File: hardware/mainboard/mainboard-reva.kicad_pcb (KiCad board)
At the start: 4 copper layers, 88 x 48 mm, 77 parts, among them J1 USB-C, J2 BATTERY, J3 SM05B-GHS-TB / ENCODER, J4 SM03B-GHS-TB / SNOOZE, J5 Molex 54550-2472 / GDEY037T03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, J6 Molex 54550-0672 / FL21 front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, J7 SPEAKER, J8 SM02B-GHS-TB / WAKE_LED, Q2 AO3400A / WAKE, U1 ESP32-S3-WROOM-1-N8, U2 BQ24074RGTR, U3 TPS62840DLCR, U4 RV-3028-C7, U5 VEML7700, U6 MAX98357AETE+T, U7 USBLC6-2SC6

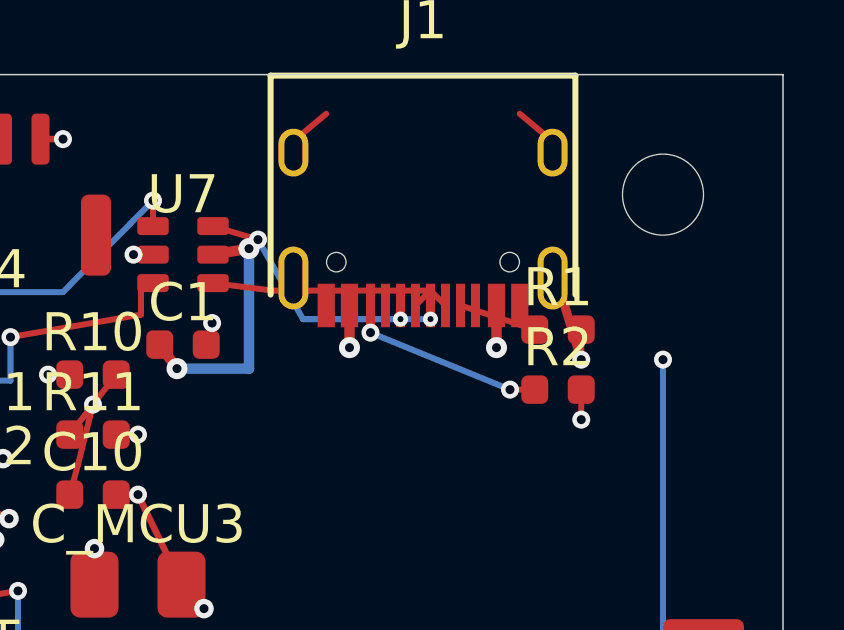
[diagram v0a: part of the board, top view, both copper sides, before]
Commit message: fix(mainboard): clean USB-C breakout lanes and CC placement
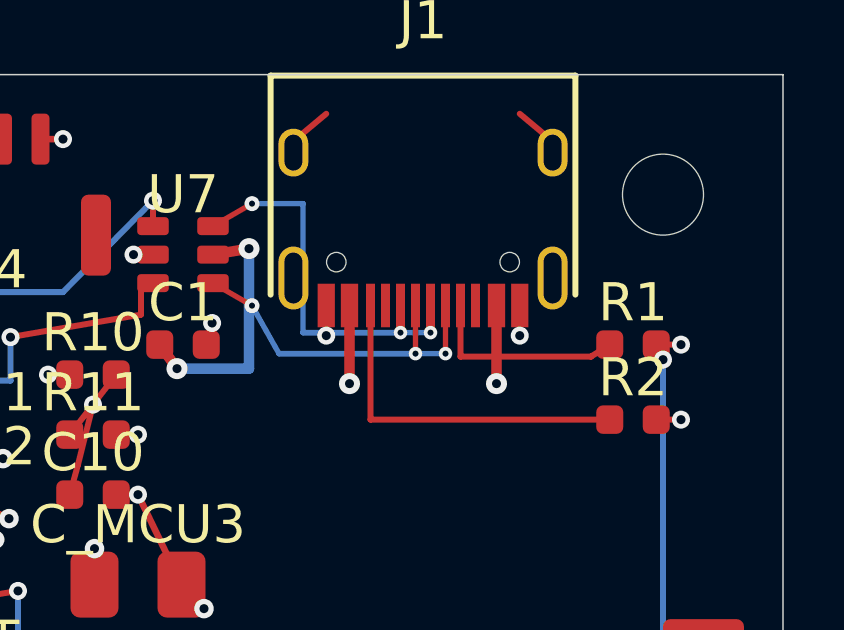
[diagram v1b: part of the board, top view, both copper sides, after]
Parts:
- moved R2 2.69 mm to (83.0, 11.5)
- moved R1 2.55 mm to (83.0, 9.00)
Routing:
- net USB_D-_CONN: track 8.67 -> 16.6 mm, vias 0 -> 3
- net USB_CC2: track 6.75 -> 11.8 mm, vias 2 -> 0
- net USB_CC1: track 2.60 -> 6.80 mm
- net USB_D+_CONN: track 13.0 -> 16.8 mm
- net VBUS_USB: track 90.6 -> 94.0 mm
- net GND: track 105.7 -> 104.1 mm, vias 52 -> 54
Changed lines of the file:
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@@
     (pad "6" smd roundrect (at 1 -0.95) (size 1.05 0.6) (layers "F.Cu" "F.Paste" "F.Mask") (roundrect_rratio 0.2) (net 59 "USB_D+_CONN"))
   )
-  (footprint "Resistor_SMD:R_0603_1608Metric" (layer "F.Cu") (at 80.5 8.5)
+  (footprint "Resistor_SMD:R_0603_1608Metric" (layer "F.Cu") (at 83.0 9.0)
     (property "Reference" "R1" (at 0 -1.4) (layer "F.SilkS"))
     (property "Value" "5.1k CC1" (at 0 1.4) (layer "F.Fab") hide)
@@
     (pad "2" smd roundrect (at 0.775 0) (size 0.9 0.95) (layers "F.Cu" "F.Paste" "F.Mask") (roundrect_rratio 0.25) (net 1 "GND"))
   )
-  (footprint "Resistor_SMD:R_0603_1608Metric" (layer "F.Cu") (at 80.5 10.5)
+  (footprint "Resistor_SMD:R_0603_1608Metric" (layer "F.Cu") (at 83.0 11.5)
     (property "Reference" "R2" (at 0 -1.4) (layer "F.SilkS"))
     (property "Value" "5.1k CC2" (at 0 1.4) (layer "F.Fab") hide)
@@
   (segment (start 24.5 20.5) (end 24.5 21.4) (width 0.20) (layer "B.Cu") (net 8))
   (segment (start 55.0 21.4) (end 55.0 21.0) (width 0.20) (layer "B.Cu") (net 8))
-  (segment (start 81.275 10.5) (end 81.275 11.5) (width 0.20) (layer "F.Cu") (net 1))
-  (via (at 81.275 11.5) (size 0.60) (drill 0.30) (layers "F.Cu" "B.Cu") (net 1))
   (via (at 20.25 16.55) (size 0.60) (drill 0.30) (layers "F.Cu" "B.Cu") (net 9))
   (segment (start 53.7 26.0) (end 55.0 26.0) (width 0.20) (layer "B.Cu") (net 9))
-  (segment (start 81.275 8.5) (end 81.275 9.5) (width 0.20) (layer "F.Cu") (net 1))
-  (via (at 81.275 9.5) (size 0.60) (drill 0.30) (layers "F.Cu" "B.Cu") (net 1))
   (segment (start 67.0 5.05) (end 67.0 4.2) (width 0.20) (layer "F.Cu") (net 10))
   (via (at 67.0 4.2) (size 0.60) (drill 0.30) (layers "F.Cu" "B.Cu") (net 10))
@@
   (segment (start 70.575 30.75) (end 72.0 31.0) (width 0.22) (layer "F.Cu") (net 1))
   (segment (start 70.575 31.25) (end 72.0 31.0) (width 0.22) (layer "F.Cu") (net 1))
-  (segment (start 80.32 6.4) (end 81.275 9.5) (width 0.3) (layer "F.Cu") (net 1))
   (segment (start 28.775 39.0) (end 28.95 42.0) (width 0.22) (layer "F.Cu") (net 1))
   (segment (start 44.725 38.5) (end 46.65 36.5) (width 0.22) (layer "F.Cu") (net 1))
@@
   (via (at 73.0 40.8) (size 0.60) (drill 0.30) (layers "F.Cu" "B.Cu") (net 42))
   (segment (start 73.0 40.8) (end 73.0 42.0) (width 0.30) (layer "F.Cu") (net 42))
-  (segment (start 77.25 7.695) (end 79.725 8.50) (width 0.20) (layer "F.Cu") (net 21))
-  (segment (start 74.25 7.695) (end 74.25 8.60) (width 0.20) (layer "F.Cu") (net 22))
-  (via (at 74.25 8.60) (size 0.60) (drill 0.30) (layers "F.Cu" "B.Cu") (net 22))
-  (segment (start 74.25 8.60) (end 78.90 10.50) (width 0.20) (layer "B.Cu") (net 22))
-  (via (at 78.90 10.50) (size 0.60) (drill 0.30) (layers "F.Cu" "B.Cu") (net 22))
-  (segment (start 78.90 10.50) (end 79.725 10.50) (width 0.20) (layer "F.Cu") (net 22))
-  (segment (start 76.25 7.695) (end 76.25 8.15) (width 0.20) (layer "F.Cu") (net 59))
-  (via (at 76.25 8.15) (size 0.50) (drill 0.20) (layers "F.Cu" "B.Cu") (net 59))
-  (segment (start 75.25 7.695) (end 75.25 8.15) (width 0.20) (layer "F.Cu") (net 59))
-  (via (at 75.25 8.15) (size 0.50) (drill 0.20) (layers "F.Cu" "B.Cu") (net 59))
-  (segment (start 76.25 8.15) (end 72.00 8.15) (width 0.20) (layer "B.Cu") (net 59))
-  (segment (start 75.25 8.15) (end 72.00 8.15) (width 0.20) (layer "B.Cu") (net 59))
-  (segment (start 72.00 8.15) (end 70.50 5.50) (width 0.20) (layer "B.Cu") (net 59))
-  (via (at 70.50 5.50) (size 0.60) (drill 0.30) (layers "F.Cu" "B.Cu") (net 59))
-  (segment (start 70.50 5.50) (end 69.0 5.05) (width 0.20) (layer "F.Cu") (net 59))
-  (segment (start 75.75 7.695) (end 76.25 7.20) (width 0.20) (layer "F.Cu") (net 60))
-  (segment (start 76.75 7.695) (end 76.25 7.20) (width 0.20) (layer "F.Cu") (net 60))
-  (segment (start 76.25 7.20) (end 71.00 7.20) (width 0.20) (layer "F.Cu") (net 60))
-  (segment (start 71.00 7.20) (end 69.0 6.95) (width 0.20) (layer "F.Cu") (net 60))
-  (segment (start 73.55 7.695) (end 73.55 9.10) (width 0.35) (layer "F.Cu") (net 2))
-  (via (at 73.55 9.10) (size 0.70) (drill 0.30) (layers "F.Cu" "B.Cu") (net 2))
-  (segment (start 78.45 7.695) (end 78.45 9.10) (width 0.35) (layer "F.Cu") (net 2))
-  (via (at 78.45 9.10) (size 0.70) (drill 0.30) (layers "F.Cu" "B.Cu") (net 2))
-  (segment (start 73.55 9.10) (end 69.80 4.60) (width 0.50) (layer "In2.Cu") (net 2))
-  (segment (start 78.45 9.10) (end 73.55 9.10) (width 0.50) (layer "In2.Cu") (net 2))
+  (segment (start 72.775 7.695) (end 72.775 8.70) (width 0.20) (layer "F.Cu") (net 1))
+  (via (at 72.775 8.70) (size 0.60) (drill 0.30) (layers "F.Cu" "B.Cu") (net 1))
+  (segment (start 79.225 7.695) (end 79.225 8.70) (width 0.20) (layer "F.Cu") (net 1))
+  (via (at 79.225 8.70) (size 0.60) (drill 0.30) (layers "F.Cu" "B.Cu") (net 1))
+  (segment (start 83.775 9.0) (end 84.6 9.0) (width 0.20) (layer "F.Cu") (net 1))
+  (via (at 84.6 9.0) (size 0.60) (drill 0.30) (layers "F.Cu" "B.Cu") (net 1))
+  (segment (start 83.775 11.5) (end 84.6 11.5) (width 0.20) (layer "F.Cu") (net 1))
+  (via (at 84.6 11.5) (size 0.60) (drill 0.30) (layers "F.Cu" "B.Cu") (net 1))
+  (segment (start 77.25 7.695) (end 77.25 9.40) (width 0.20) (layer "F.Cu") (net 21))
+  (segment (start 77.25 9.40) (end 81.60 9.40) (width 0.20) (layer "F.Cu") (net 21))
+  (segment (start 81.60 9.40) (end 82.225 9.00) (width 0.20) (layer "F.Cu") (net 21))
+  (segment (start 74.25 7.695) (end 74.25 11.50) (width 0.20) (layer "F.Cu") (net 22))
+  (segment (start 74.25 11.50) (end 82.225 11.50) (width 0.20) (layer "F.Cu") (net 22))
+  (segment (start 75.25 7.695) (end 75.25 8.60) (width 0.18) (layer "F.Cu") (net 59))
+  (via (at 75.25 8.60) (size 0.45) (drill 0.20) (layers "F.Cu" "B.Cu") (net 59))
+  (segment (start 76.25 7.695) (end 76.25 8.60) (width 0.18) (layer "F.Cu") (net 59))
+  (via (at 76.25 8.60) (size 0.45) (drill 0.20) (layers "F.Cu" "B.Cu") (net 59))
+  (segment (start 75.25 8.60) (end 72.00 8.60) (width 0.18) (layer "B.Cu") (net 59))
+  (segment (start 76.25 8.60) (end 72.00 8.60) (width 0.18) (layer "B.Cu") (net 59))
+  (segment (start 72.00 8.60) (end 72.00 4.30) (width 0.18) (layer "B.Cu") (net 59))
+  (segment (start 72.00 4.30) (end 70.30 4.30) (width 0.18) (layer "B.Cu") (net 59))
+  (via (at 70.30 4.30) (size 0.50) (drill 0.20) (layers "F.Cu" "B.Cu") (net 59))
+  (segment (start 70.30 4.30) (end 69.0 5.05) (width 0.18) (layer "F.Cu") (net 59))
+  (segment (start 75.75 7.695) (end 75.75 9.30) (width 0.18) (layer "F.Cu") (net 60))
+  (via (at 75.75 9.30) (size 0.45) (drill 0.20) (layers "F.Cu" "B.Cu") (net 60))
+  (segment (start 76.75 7.695) (end 76.75 9.30) (width 0.18) (layer "F.Cu") (net 60))
+  (via (at 76.75 9.30) (size 0.45) (drill 0.20) (layers "F.Cu" "B.Cu") (net 60))
+  (segment (start 75.75 9.30) (end 71.20 9.30) (width 0.18) (layer "B.Cu") (net 60))
+  (segment (start 76.75 9.30) (end 71.20 9.30) (width 0.18) (layer "B.Cu") (net 60))
+  (segment (start 71.20 9.30) (end 70.30 7.70) (width 0.18) (layer "B.Cu") (net 60))
+  (via (at 70.30 7.70) (size 0.50) (drill 0.20) (layers "F.Cu" "B.Cu") (net 60))
+  (segment (start 70.30 7.70) (end 69.0 6.95) (width 0.18) (layer "F.Cu") (net 60))
+  (segment (start 73.55 7.695) (end 73.55 10.30) (width 0.35) (layer "F.Cu") (net 2))
+  (via (at 73.55 10.30) (size 0.70) (drill 0.30) (layers "F.Cu" "B.Cu") (net 2))
+  (segment (start 78.45 7.695) (end 78.45 10.30) (width 0.35) (layer "F.Cu") (net 2))
+  (via (at 78.45 10.30) (size 0.70) (drill 0.30) (layers "F.Cu" "B.Cu") (net 2))
+  (segment (start 78.45 10.30) (end 73.55 10.30) (width 0.50) (layer "In2.Cu") (net 2))
+  (segment (start 73.55 10.30) (end 69.80 4.60) (width 0.50) (layer "In2.Cu") (net 2))
   (segment (start 69.0 6.0) (end 70.20 5.80) (width 0.35) (layer "F.Cu") (net 2))
   (via (at 70.20 5.80) (size 0.70) (drill 0.30) (layers "F.Cu" "B.Cu") (net 2))

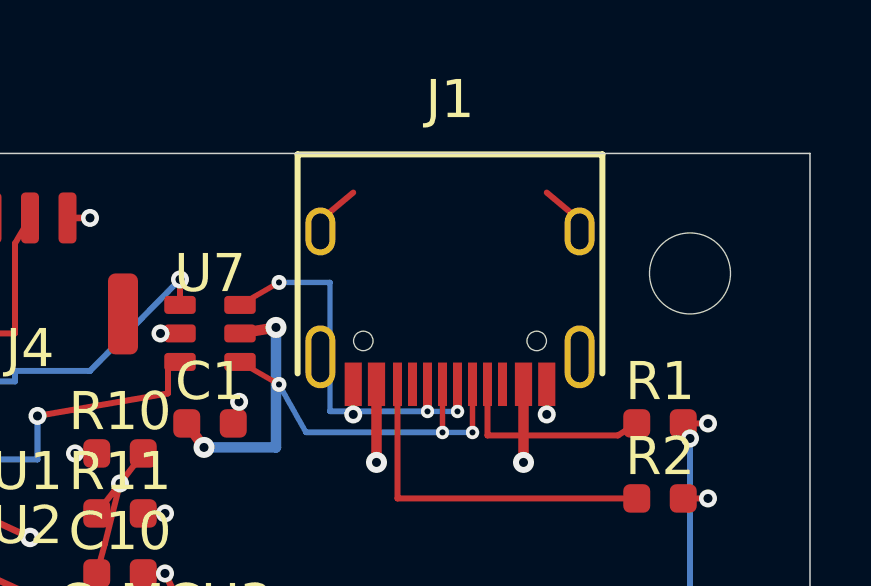
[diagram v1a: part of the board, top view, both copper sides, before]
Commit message: fix(mainboard): align USB-C embedded footprint to official datum
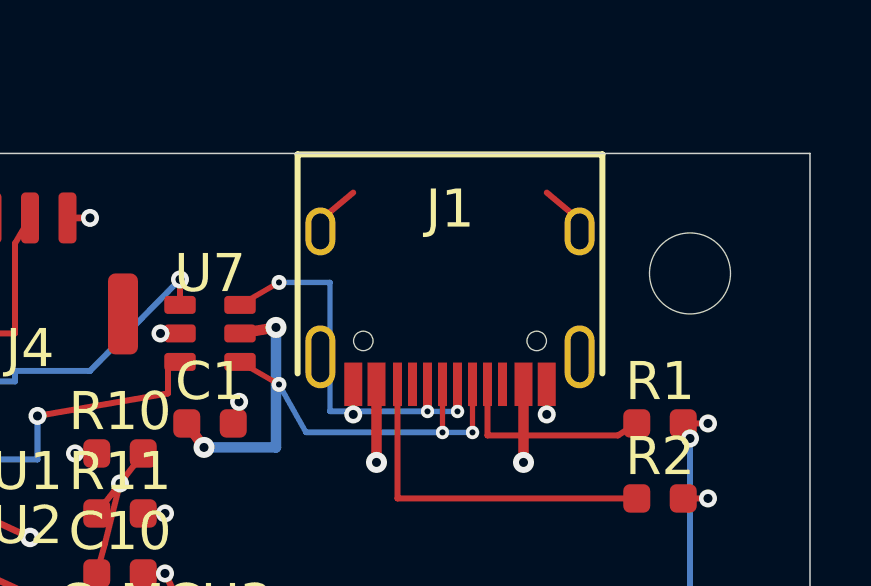
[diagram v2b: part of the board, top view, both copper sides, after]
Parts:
- moved J1 3.65 mm to (76.0, 3.65)
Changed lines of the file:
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@@
     (property "Reference" "H4" (at 0 -2.5) (layer "F.SilkS") hide)
     (pad "" np_thru_hole circle (at 0 0) (size 2.7 2.7) (drill 2.7) (layers "*.Cu" "*.Mask")))
-  (footprint "ENKU_Clock:HRO-TYPE-C-31-M-12" (layer "F.Cu") (at 76 0 180)
+  (footprint "ENKU_Clock:HRO-TYPE-C-31-M-12" (layer "F.Cu") (at 76 3.65 180)
     (property "Reference" "J1" (at 0 1.8) (layer "F.SilkS"))
     (property "Value" "USB-C" (at 0 1.15) (layer "F.Fab") hide)
     (attr smd)
-    (fp_line (start -5.08 -0.033) (end -5.08 -7.333) (stroke (width 0.20) (type solid)) (layer "F.SilkS"))
-    (fp_line (start -5.08 -0.033) (end 5.08 -0.033) (stroke (width 0.20) (type solid)) (layer "F.SilkS"))
-    (fp_line (start 5.08 -0.033) (end 5.08 -7.333) (stroke (width 0.20) (type solid)) (layer "F.SilkS"))
-    (pad "" np_thru_hole circle (at -2.89 -6.25) (size 0.65 0.65) (drill 0.65) (layers "*.Cu" "*.Mask"))
-    (pad "" np_thru_hole circle (at 2.89 -6.25) (size 0.65 0.65) (drill 0.65) (layers "*.Cu" "*.Mask"))
-    (pad "A1" smd rect (at -3.225 -7.695) (size 0.575 1.45) (layers "F.Cu" "F.Paste" "F.Mask") (net 1 "GND"))
-    (pad "A4" smd rect (at -2.45 -7.695) (size 0.575 1.45) (layers "F.Cu" "F.Paste" "F.Mask") (net 2 "VBUS_USB"))
-    (pad "A5" smd rect (at -1.25 -7.695) (size 0.3 1.45) (layers "F.Cu" "F.Paste" "F.Mask") (net 21 "USB_CC1"))
-    (pad "A6" smd rect (at -0.25 -7.695) (size 0.3 1.45) (layers "F.Cu" "F.Paste" "F.Mask") (net 59 "USB_D+_CONN"))
-    (pad "A7" smd rect (at 0.25 -7.695) (size 0.3 1.45) (layers "F.Cu" "F.Paste" "F.Mask") (net 60 "USB_D-_CONN"))
-    (pad "A8" smd rect (at 1.25 -7.695) (size 0.3 1.45) (layers "F.Cu" "F.Paste" "F.Mask"))
-    (pad "A9" smd rect (at 2.45 -7.695) (size 0.575 1.45) (layers "F.Cu" "F.Paste" "F.Mask") (net 2 "VBUS_USB"))
-    (pad "A12" smd rect (at 3.225 -7.695) (size 0.575 1.45) (layers "F.Cu" "F.Paste" "F.Mask") (net 1 "GND"))
-    (pad "B5" smd rect (at 1.75 -7.695) (size 0.3 1.45) (layers "F.Cu" "F.Paste" "F.Mask") (net 22 "USB_CC2"))
-    (pad "B6" smd rect (at 0.75 -7.695) (size 0.3 1.45) (layers "F.Cu" "F.Paste" "F.Mask") (net 59 "USB_D+_CONN"))
-    (pad "B7" smd rect (at -0.75 -7.695) (size 0.3 1.45) (layers "F.Cu" "F.Paste" "F.Mask") (net 60 "USB_D-_CONN"))
-    (pad "B8" smd rect (at -1.75 -7.695) (size 0.3 1.45) (layers "F.Cu" "F.Paste" "F.Mask"))
-    (pad "S1" thru_hole oval (at -4.32 -6.78) (size 1 2.1) (drill oval 0.6 1.7) (layers "*.Cu" "*.Mask") (net 1 "GND"))
-    (pad "S1" thru_hole oval (at -4.32 -2.6) (size 1 1.6) (drill oval 0.6 1.2) (layers "*.Cu" "*.Mask") (net 1 "GND"))
-    (pad "S1" thru_hole oval (at 4.32 -6.78) (size 1 2.1) (drill oval 0.6 1.7) (layers "*.Cu" "*.Mask") (net 1 "GND"))
-    (pad "S1" thru_hole oval (at 4.32 -2.6) (size 1 1.6) (drill oval 0.6 1.2) (layers "*.Cu" "*.Mask") (net 1 "GND"))
+    (fp_line (start -5.08 3.617) (end -5.08 -3.683) (stroke (width 0.20) (type solid)) (layer "F.SilkS"))
+    (fp_line (start -5.08 3.617) (end 5.08 3.617) (stroke (width 0.20) (type solid)) (layer "F.SilkS"))
+    (fp_line (start 5.08 3.617) (end 5.08 -3.683) (stroke (width 0.20) (type solid)) (layer "F.SilkS"))
+    (pad "" np_thru_hole circle (at -2.89 -2.60) (size 0.65 0.65) (drill 0.65) (layers "*.Cu" "*.Mask"))
+    (pad "" np_thru_hole circle (at 2.89 -2.60) (size 0.65 0.65) (drill 0.65) (layers "*.Cu" "*.Mask"))
+    (pad "A1" smd rect (at -3.225 -4.045) (size 0.6 1.45) (layers "F.Cu" "F.Paste" "F.Mask") (net 1 "GND"))
+    (pad "A4" smd rect (at -2.45 -4.045) (size 0.6 1.45) (layers "F.Cu" "F.Paste" "F.Mask") (net 2 "VBUS_USB"))
+    (pad "A5" smd rect (at -1.25 -4.045) (size 0.3 1.45) (layers "F.Cu" "F.Paste" "F.Mask") (net 21 "USB_CC1"))
+    (pad "A6" smd rect (at -0.25 -4.045) (size 0.3 1.45) (layers "F.Cu" "F.Paste" "F.Mask") (net 59 "USB_D+_CONN"))
+    (pad "A7" smd rect (at 0.25 -4.045) (size 0.3 1.45) (layers "F.Cu" "F.Paste" "F.Mask") (net 60 "USB_D-_CONN"))
+    (pad "A8" smd rect (at 1.25 -4.045) (size 0.3 1.45) (layers "F.Cu" "F.Paste" "F.Mask"))
+    (pad "A9" smd rect (at 2.45 -4.045) (size 0.6 1.45) (layers "F.Cu" "F.Paste" "F.Mask") (net 2 "VBUS_USB"))
+    (pad "A12" smd rect (at 3.225 -4.045) (size 0.6 1.45) (layers "F.Cu" "F.Paste" "F.Mask") (net 1 "GND"))
+    (pad "B5" smd rect (at 1.75 -4.045) (size 0.3 1.45) (layers "F.Cu" "F.Paste" "F.Mask") (net 22 "USB_CC2"))
+    (pad "B6" smd rect (at 0.75 -4.045) (size 0.3 1.45) (layers "F.Cu" "F.Paste" "F.Mask") (net 59 "USB_D+_CONN"))
+    (pad "B7" smd rect (at -0.75 -4.045) (size 0.3 1.45) (layers "F.Cu" "F.Paste" "F.Mask") (net 60 "USB_D-_CONN"))
+    (pad "B8" smd rect (at -1.75 -4.045) (size 0.3 1.45) (layers "F.Cu" "F.Paste" "F.Mask"))
+    (pad "S1" thru_hole oval (at -4.32 -3.13) (size 1 2.1) (drill oval 0.6 1.7) (layers "*.Cu" "*.Mask") (net 1 "GND"))
+    (pad "S1" thru_hole oval (at -4.32 1.05) (size 1 1.6) (drill oval 0.6 1.2) (layers "*.Cu" "*.Mask") (net 1 "GND"))
+    (pad "S1" thru_hole oval (at 4.32 -3.13) (size 1 2.1) (drill oval 0.6 1.7) (layers "*.Cu" "*.Mask") (net 1 "GND"))
+    (pad "S1" thru_hole oval (at 4.32 1.05) (size 1 1.6) (drill oval 0.6 1.2) (layers "*.Cu" "*.Mask") (net 1 "GND"))
   )
   (footprint "Connector_JST:JST_PH_S3B-PH-K_1x03_P2.00mm_Horizontal" (layer "F.Cu") (at 7 10)
